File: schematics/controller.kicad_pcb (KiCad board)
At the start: 2 copper layers, 58.8 x 81.5 mm, 48 parts, among them J1 Conn_LoadCell, J2 Conn_Display, J3 Conn_UART, J4 Conn_LiPo, P1 USB-C-6Pin, Q1 MMBT4403, Q2 IRLML6402, SW1 SW_EN, SW2 SW_Boot, SW3 RotaryEncoder_Switch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

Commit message: Updated pcb
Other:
- rule pad_to_mask_clearance: 0 -> 0.05
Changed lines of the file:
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@@
       (dielectric_constraints no)
     )
-    (pad_to_mask_clearance 0)
+    (pad_to_mask_clearance 0.05)
     (pcbplotparams
       (layerselection 0x00010fc_ffffffff)

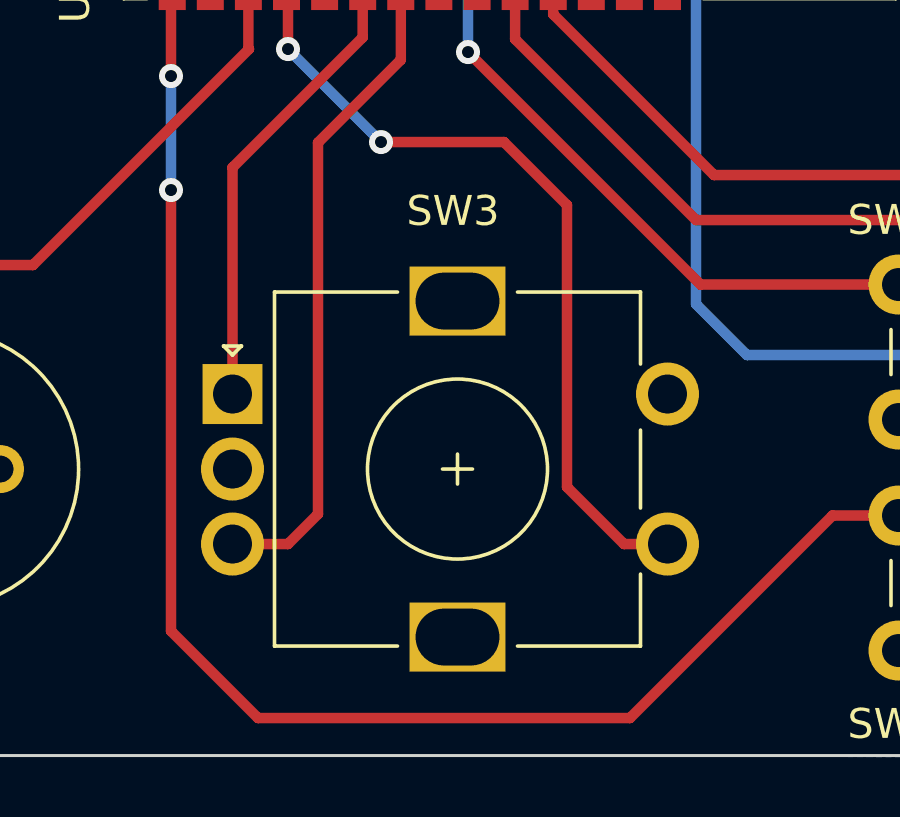
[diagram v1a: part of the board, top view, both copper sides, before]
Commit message: Updated voltage divider for hx711 in schematic
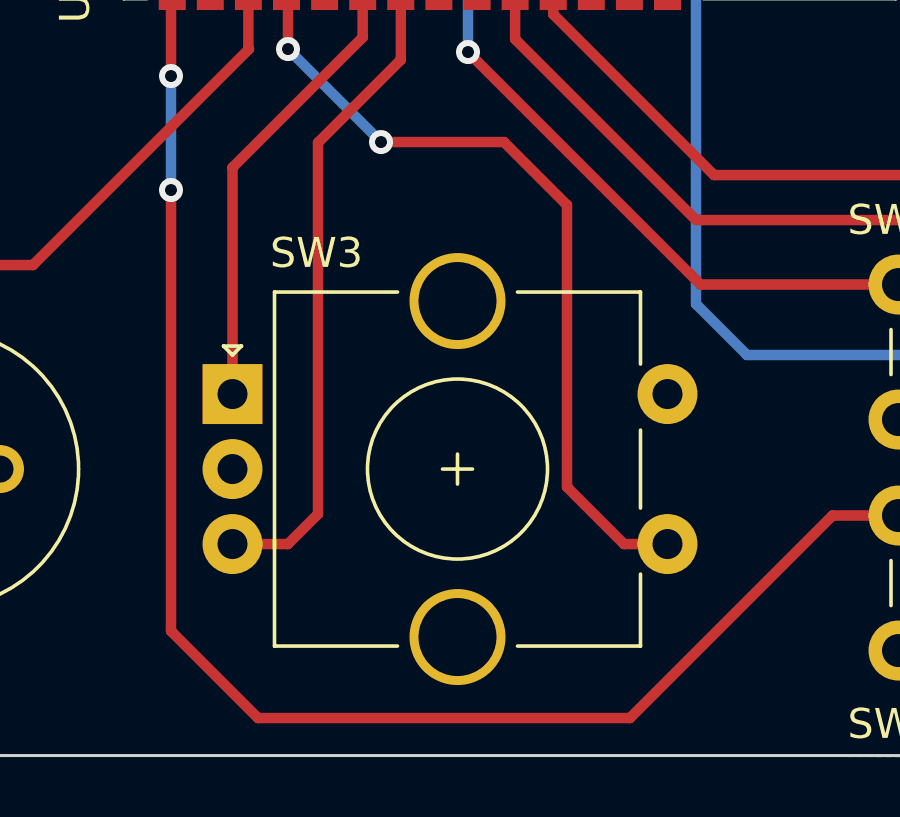
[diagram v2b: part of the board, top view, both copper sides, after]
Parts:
- R6: value 20k -> 10k
- SW3: footprint Custom:RotaryEncoder_Aliexpress_Alps_EC11E-Switch_Vertical_H20mm -> Rotary_Encoder:RotaryEncoder_Alps_EC11E-Switch_Vertical_H20mm_CircularMountingHoles

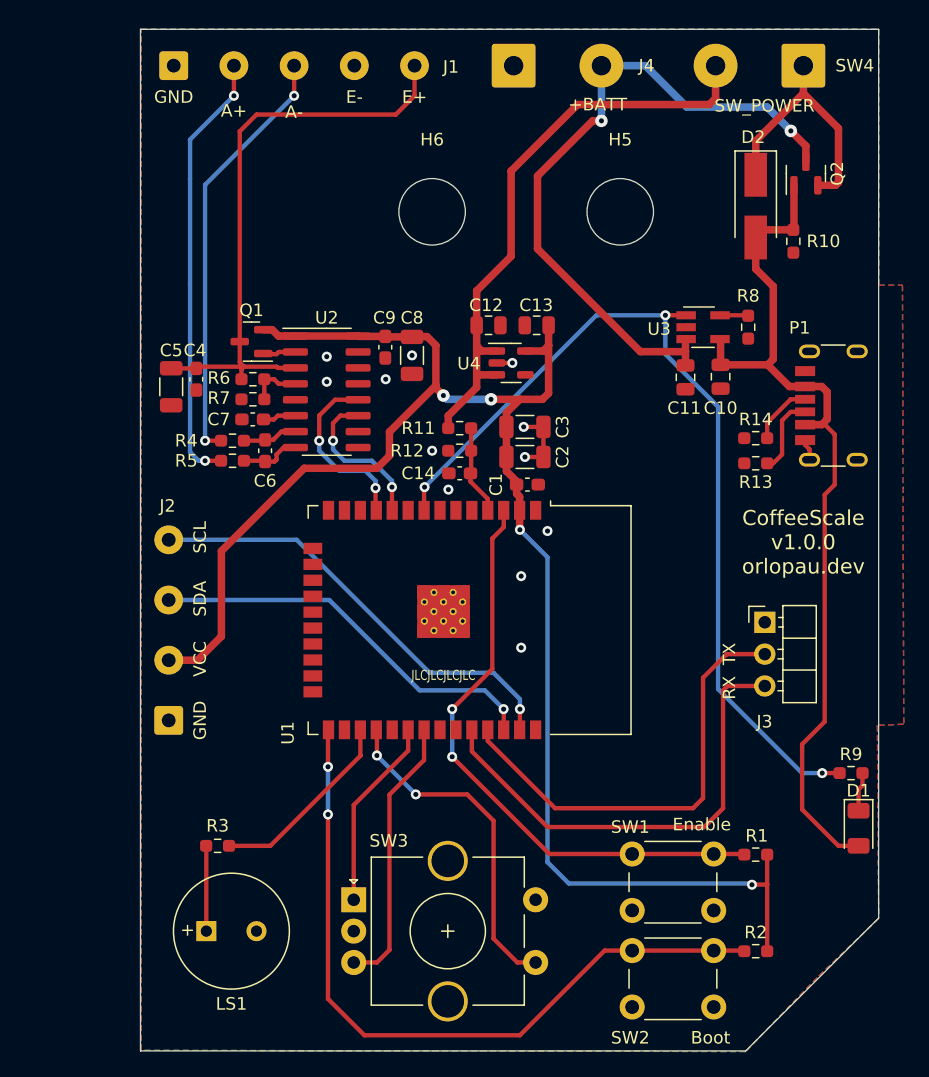
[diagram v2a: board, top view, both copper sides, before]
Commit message: Updated schematic to v1.1.0
* Added TVS diode for USB connector
* Added active buzzer instead of passive piezo buzzer
* Added battery protection IC
* Changed location of enable button, enabling the mounting of a button which is visible externally
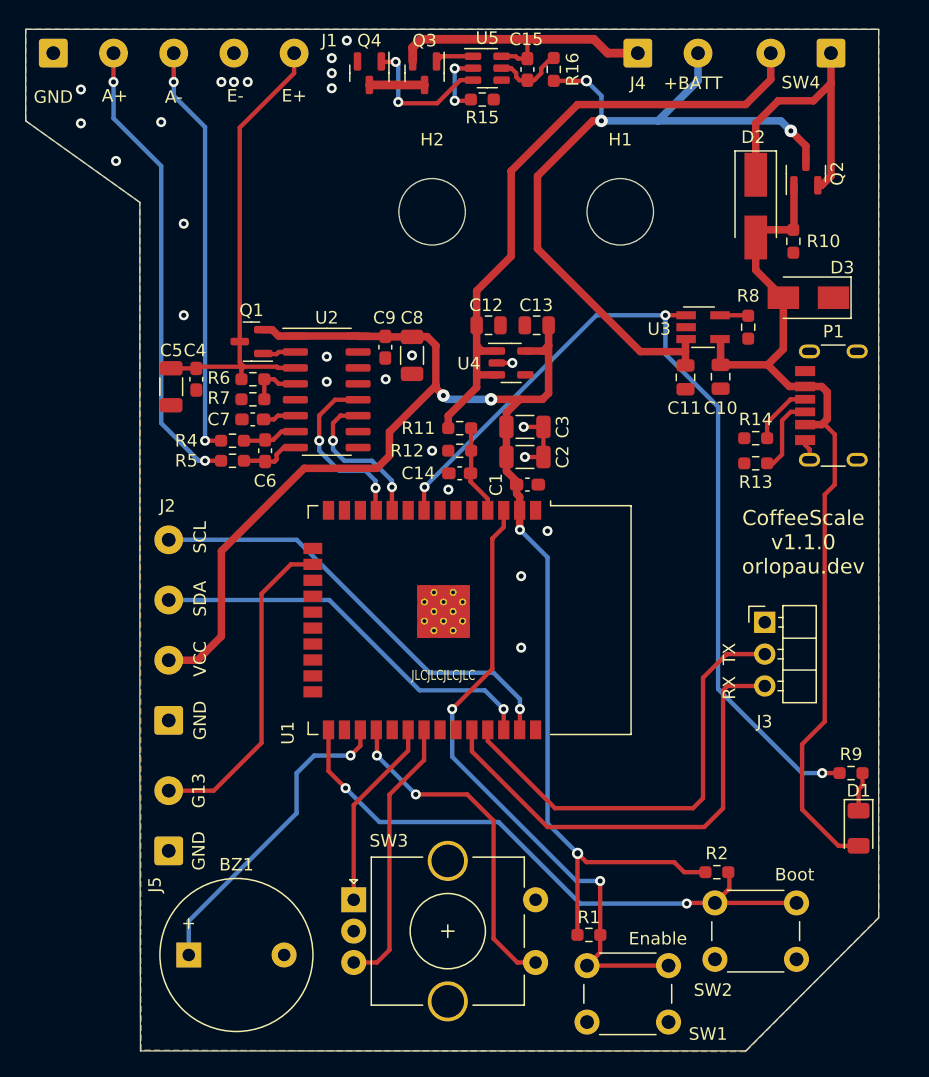
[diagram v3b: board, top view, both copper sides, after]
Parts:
- removed LS1: Speaker_Crystal, Buzzer_Beeper:MagneticBuzzer_PUI_AT-0927-TT-6-R
- removed R3: 220, Resistor_SMD:R_0603_1608Metric_Pad0.98x0.95mm_HandSolder
- added BZ1: Buzzer, Buzzer_Beeper:Buzzer_12x9.5RM7.6, F.Cu at (90.6, 163.9)
- added C15: 0.1uF, Capacitor_SMD:C_0603_1608Metric_Pad1.08x0.95mm_HandSolder, F.Cu at (117.6, 93.3)
- added D3: SMAJ6.0CA, Diode_SMD:D_SMA, F.Cu at (140.0, 111.5)
- added J5: Conn_G13, Connector_Wire:SolderWire-0.5sqmm_1x02_P4.8mm_D0.9mm_OD2.3mm, F.Cu at (89.0, 155.6)
- added Q3: IRLML2502, Package_TO_SOT_SMD:SOT-23, F.Cu at (109.4, 93.6)
- added Q4: IRLML2502, Package_TO_SOT_SMD:SOT-23, F.Cu at (105.0, 93.6)
- added R15: 2.7k, Resistor_SMD:R_0603_1608Metric_Pad0.98x0.95mm_HandSolder, F.Cu at (114.0, 95.7)
- added R16: 330, Resistor_SMD:R_0603_1608Metric_Pad0.98x0.95mm_HandSolder, F.Cu at (119.7, 93.3)
- added U5: AP9101CK6, Package_TO_SOT_SMD:SOT-23-6, F.Cu at (114.4, 93.2)
- J4, SW4: footprint Connector_Wire:SolderWire-0.75sqmm_1x02_P7mm_D1.25mm_OD3.5mm -> Connector_Wire:SolderWire-0.5sqmm_1x02_P4.8mm_D0.9mm_OD2.3mm
- moved R1 14.8 mm to (122.5, 162.3), turned to 0 degrees
- moved J4 9.95 mm to (126.4, 92.0)
- moved J1 9.65 mm to (79.8, 92.0)
- moved SW1 9.60 mm to (128.8, 169.2)
- moved SW2 7.62 mm to (132.6, 159.8)
- moved R2 7.02 mm to (132.7, 157.3), turned to 0 degrees
- moved SW4 2.42 mm to (141.8, 92.0)
- renumbered H5 to H1, H6 to H2
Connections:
- J4 pad 1: GND -> -BATT
- U1 pad 16: unconnected-(U1-Pad16) -> G13
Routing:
- net G13: track 0.00 -> 25.9 mm
- net -BATT: track 0.00 -> 23.5 mm
- net /CO: track 0.00 -> 11.0 mm, vias 0 -> 2
- net Net-(R2-Pad2): track 58.7 -> 48.0 mm
- net Net-(U1-Pad27): track 15.5 -> 25.3 mm, vias 0 -> 1
- net /E+: track 47.5 -> 38.0 mm
- net +3.3V: track 134.8 -> 126.5 mm
- net Net-(LS1-Pad1): track 6.81 -> 0.00 mm
- net +BATT: track 54.6 -> 61.4 mm, vias 2 -> 3
- net Net-(C15-Pad1): track 0.00 -> 5.71 mm
- net /VM: track 0.00 -> 5.38 mm, vias 0 -> 2
- net /SW_Out: track 47.3 -> 51.8 mm
- net Net-(Q3-Pad3): track 0.00 -> 4.40 mm
- net /DO: track 0.00 -> 3.08 mm
- net Net-(R1-Pad2): track 47.9 -> 50.9 mm
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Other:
- board size 58.8 x 81.5 mm -> 68 x 81.5 mm
- rule pad_to_mask_clearance: 0.05 -> 0
- board text added: "CoffeeScale v1.1.0 orlopau.dev"
- board text added: "G13"
- board text removed: "CoffeeScale v1.0.0 orlopau.dev"
- board text removed: "SW_POWER"

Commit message: Changed circular mounting holes to eliptical for rotary encoder
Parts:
- SW3: footprint Rotary_Encoder:RotaryEncoder_Alps_EC11E-Switch_Vertical_H20mm_CircularMountingHoles -> Rotary_Encoder:RotaryEncoder_Alps_EC11E-Switch_Vertical_H20mm
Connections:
- net /A+ renamed Net-(J1-Pad2)
- net /A- renamed Net-(J1-Pad3)
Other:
- board text added: "CoffeeScale v1.1.1 orlopau.dev"
- board text removed: "CoffeeScale v1.1.0 orlopau.dev"

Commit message: wip
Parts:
- removed R16: 330, Resistor_SMD:R_0603_1608Metric_Pad0.98x0.95mm_HandSolder
- added R3: 100, Resistor_SMD:R_0603_1608Metric_Pad0.98x0.95mm_HandSolder, F.Cu at (119.7, 93.3)
- R15: value 2.7k -> 1k
- U3: footprint Package_TO_SOT_SMD:SOT-23-5_HandSoldering -> Package_TO_SOT_SMD:SOT-23-5
- U5: value AP9101CK6 -> DW01-P; footprint Package_TO_SOT_SMD:SOT-23-6 -> Package_TO_SOT_SMD:SOT-23-6_Handsoldering
- moved R15 1.25 mm to (114.4, 96.9), turned to -90 degrees
- moved C15 0.32 mm to (117.9, 93.2)
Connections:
- net /CO renamed /OC
- net /DO renamed /OD
- R15 pad 1: GND -> Net-(U5-CS)
- R15 pad 2: /VM -> GND
- U5 pad 2: /VM -> Net-(U5-CS)
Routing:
- net /VM: track 5.38 -> 0.00 mm, vias 2 -> 0
- net Net-(U5-CS): track 0.00 -> 4.04 mm

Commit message: Changed lipo protection IC to DW01, added LCSC part numbers
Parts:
- D2: value D_Schottky -> 1N5819
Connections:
- net Net-(J1-Pin_2) renamed /A+
- net Net-(J1-Pin_3) renamed /A-
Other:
- board text added: "CoffeeScale v1.2.1 orlopau.dev"
- board text removed: "CoffeeScale v1.1.1 orlopau.dev"
